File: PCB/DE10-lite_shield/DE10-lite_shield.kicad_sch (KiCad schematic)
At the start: 4 parts

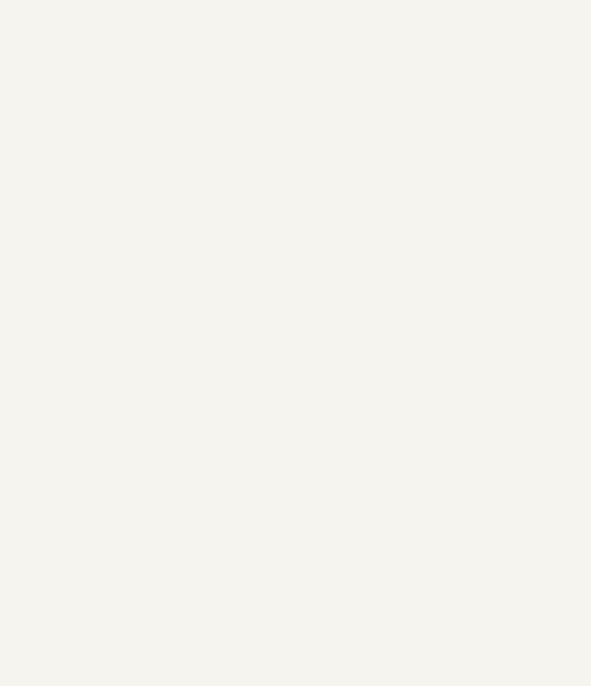
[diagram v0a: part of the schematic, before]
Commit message: Updated PCB dimensions
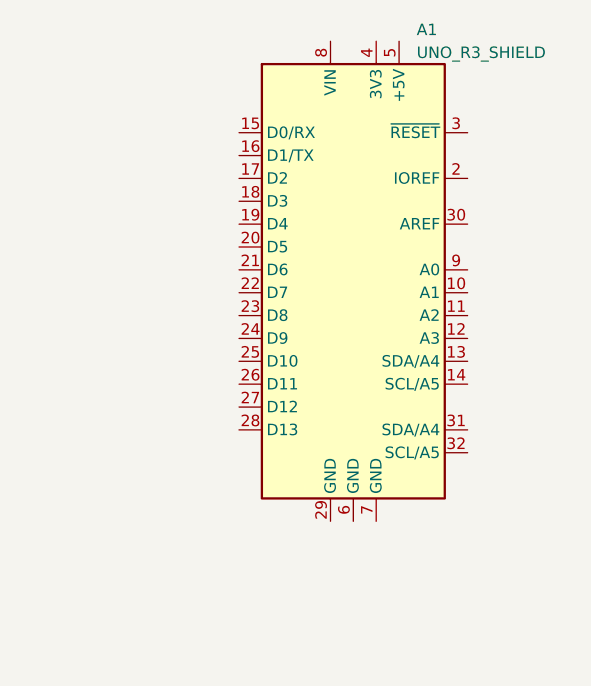
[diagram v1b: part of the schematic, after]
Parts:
- added A1: UNO_R3_SHIELD, footprints:UNO_R3_SHIELD, symbol Personal Library:UNO_R3_SHIELD
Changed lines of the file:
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@@
+    )
+  )
+  (symbol (lib_id "Personal Library:UNO_R3_SHIELD") (at 118.11 97.79 0) (unit 1)
+    (in_bom yes) (on_board yes) (dnp no) (fields_autoplaced)
+    (property "Reference" "A1" (at 125.1459 71.12 0)
+      (effects (font (size 1.27 1.27)) (justify left))
+    )
+    (property "Value" "UNO_R3_SHIELD" (at 125.1459 73.66 0)
+      (effects (font (size 1.27 1.27)) (justify left))
+    )
+    (property "Footprint" "footprints:UNO_R3_SHIELD" (at 118.11 97.79 0)
+      (effects (font (size 1.27 1.27) italic) hide)
+    )
+    (property "Datasheet" "https://www.arduino.cc/en/Main/arduinoBoardUno" (at 118.11 97.79 0)
+      (effects (font (size 1.27 1.27)) hide)
+    )
+    (pin "1")
+    (pin "10")
+    (pin "11")
+    (pin "12")
+    (pin "13")
+    (pin "14")
+    (pin "15")
+    (pin "16")
+    (pin "17")
+    (pin "18")
+    (pin "19")
+    (pin "2")
+    (pin "20")
+    (pin "21")
+    (pin "22")
+    (pin "23")
+    (pin "24")
+    (pin "25")
+    (pin "26")
+    (pin "27")
+    (pin "28")
+    (pin "29")
+    (pin "3")
+    (pin "30")
+    (pin "31")
+    (pin "32")
+    (pin "4")
+    (pin "5")
+    (pin "6")
+    (pin "7")
+    (pin "8")
+    (pin "9")
+    (instances
+      (project "DE10-lite_shield"
+        (path "/42dcd1c6-b27b-471e-adaa-a184b6e8160d"
+          (reference "A1") (unit 1)
+        )
+      )
     )
   )

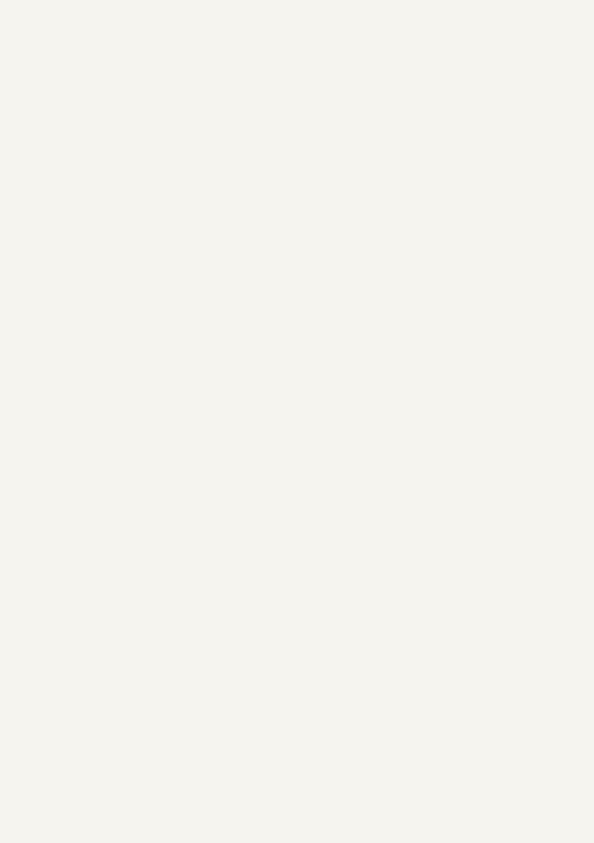
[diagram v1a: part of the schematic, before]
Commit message: Updated .gitignore
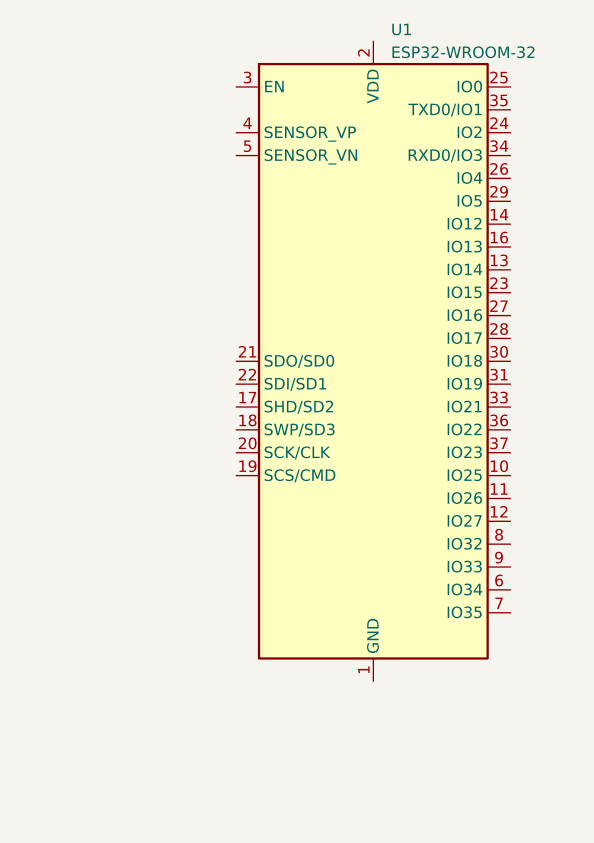
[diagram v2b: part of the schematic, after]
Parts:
- added U1: ESP32-WROOM-32, RF_Module:ESP32-WROOM-32, symbol RF_Module:ESP32-WROOM-32
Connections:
- new net: U1.1 (GND), U1.15 (GND), U1.38 (GND), U1.39 (GND)
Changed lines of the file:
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@@
+    )
+  )
+  (symbol (lib_id "RF_Module:ESP32-WROOM-32") (at 198.12 93.98 0) (unit 1)
+    (in_bom yes) (on_board yes) (dnp no) (fields_autoplaced)
+    (property "Reference" "U1" (at 200.0759 57.15 0)
+      (effects (font (size 1.27 1.27)) (justify left))
+    )
+    (property "Value" "ESP32-WROOM-32" (at 200.0759 59.69 0)
+      (effects (font (size 1.27 1.27)) (justify left))
+    )
+    (property "Footprint" "RF_Module:ESP32-WROOM-32" (at 198.12 132.08 0)
+      (effects (font (size 1.27 1.27)) hide)
+    )
+    (property "Datasheet" "https://www.espressif.com/sites/default/files/documentation/esp32-wroom-32_datasheet_en.pdf" (at 190.5 92.71 0)
+      (effects (font (size 1.27 1.27)) hide)
+    )
+    (pin "1")
+    (pin "10")
+    (pin "11")
+    (pin "12")
+    (pin "13")
+    (pin "14")
+    (pin "15")
+    (pin "16")
+    (pin "17")
+    (pin "18")
+    (pin "19")
+    (pin "2")
+    (pin "20")
+    (pin "21")
+    (pin "22")
+    (pin "23")
+    (pin "24")
+    (pin "25")
+    (pin "26")
+    (pin "27")
+    (pin "28")
+    (pin "29")
+    (pin "3")
+    (pin "30")
+    (pin "31")
+    (pin "32")
+    (pin "33")
+    (pin "34")
+    (pin "35")
+    (pin "36")
+    (pin "37")
+    (pin "38")
+    (pin "39")
+    (pin "4")
+    (pin "5")
+    (pin "6")
+    (pin "7")
+    (pin "8")
+    (pin "9")
+    (instances
+      (project "DE10-lite_shield"
+        (path "/42dcd1c6-b27b-471e-adaa-a184b6e8160d"
+          (reference "U1") (unit 1)
+        )
+      )
     )
   )

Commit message: PCB almost done
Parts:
- added A2, A3: Pololu_Breakout_A4988, Module:Pololu_Breakout-16_15.2x20.3mm, symbol Driver_Motor:Pololu_Breakout_A4988
- added C1, C2: 100u, Capacitor_THT:C_Rect_L4.0mm_W2.5mm_P2.50mm, symbol Device:C_Polarized_Small
- added C10, C11, C19, C20: 10n, Capacitor_SMD:C_0402_1005Metric, symbol Device:C_Small
- added C12, C14, C17, C18, C22, C23, C3, C4: 100n, Capacitor_SMD:C_0402_1005Metric, symbol Device:C_Small
- added C13: 4u7, Capacitor_SMD:C_0402_1005Metric, symbol Device:C_Small
- added C15, C16, C21, C24, C8, C9: 10u, Capacitor_SMD:C_0402_1005Metric, symbol Device:C_Small
- added C5: 1u, Capacitor_SMD:C_0402_1005Metric, symbol Device:C_Small
- added C6, C7: 47u, Capacitor_SMD:C_0805_2012Metric, symbol Device:C_Small
- added D1: BAT760-115, Diode_SMD:D_SOD-323, symbol Device:D_Schottky
- added D2, D3: LED_R, LED_SMD:LED_0603_1608Metric, symbol Device:LED_Small
- added D4, D5: LED_B, LED_SMD:LED_0603_1608Metric, symbol Device:LED_Small
- added F1: Fuse, Fuse:Fuseholder_Cylinder-5x20mm_Schurter_0031_8201_Horizontal_Open, symbol Device:Fuse
- added J1, J2: Conn_01x04, Connector_PinHeader_2.54mm:PinHeader_1x04_P2.54mm_Vertical, symbol Connector_Generic:Conn_01x04
- added J10: Conn_01x02, Connector_PinHeader_2.54mm:PinHeader_1x02_P2.54mm_Vertical, symbol Connector_Generic:Conn_01x02
- added J11, J12: SM04B-SRSS-TB(LF)(SN), footprints:JST_SM04B-SRSS-TB(LF)(SN), symbol SM04B-SRSS-TB_LF__SN_:SM04B-SRSS-TB(LF)(SN)
- added J3: Screw_Terminal_01x02, TerminalBlock:TerminalBlock_bornier-2_P5.08mm, symbol Connector:Screw_Terminal_01x02
- added J4: USB4056-03-A, footprints:GCT_USB4056-03-A_REVA, symbol USB4056-03-A:USB4056-03-A
- added J5, J6, J7, J8: Conn_01x05, Connector_PinHeader_2.54mm:PinHeader_1x05_P2.54mm_Vertical, symbol Connector_Generic:Conn_01x05
- added J9: Conn_01x03, Connector_PinHeader_2.54mm:PinHeader_1x03_P2.54mm_Vertical, symbol Connector_Generic:Conn_01x03
- added JP1, JP2, JP3, JP4, JP5, JP6, JP7, JP8: Jumper_2_Open, Connector_PinHeader_2.54mm:PinHeader_1x02_P2.54mm_Vertical, symbol Jumper:Jumper_2_Open
- added L1: 3u3, footprints:INDPM3630X200N, symbol Device:L_Small
- added L2: 2u2, footprints:INDPM3630X200N, symbol Device:L_Small
- added Q1, Q2: S8050, footprints:S8050, symbol Transistor_BJT:S8050
- added R1, R2: R_Small, Resistor_SMD:R_0402_1005Metric, symbol Device:R_Small
- added R10, R30, R5, R6: 4k7, Resistor_SMD:R_0402_1005Metric, symbol Device:R_Small
- added R11, R12, R13, R14, R15, R18, R20, R21, R22, R23, R27, R31, R4, R7, R8: 10k, Resistor_SMD:R_0402_1005Metric, symbol Device:R_Small
- added R16, R17, R24, R9: 2k2, Resistor_SMD:R_0402_1005Metric, symbol Device:R_Small
- added R19: 3k3, Resistor_SMD:R_0402_1005Metric, symbol Device:R_Small
- added R25, R26, R28: 1k5, Resistor_SMD:R_0402_1005Metric, symbol Device:R_Small
- added R3: 33k, Resistor_SMD:R_0402_1005Metric, symbol Device:R_Small
- added S1, S2: TS20-42-25-WT-160-SMT-TR, footprints:TS204225WT160SMTTR, symbol TS20-42-25-WT-160-SMT-TR:TS20-42-25-WT-160-SMT-TR
- added SW1: SW_DPDT_x2, Connector_PinHeader_2.54mm:PinHeader_1x03_P2.54mm_Vertical, symbol Switch:SW_DPDT_x2
- added U2: CP2102N-Axx-xQFN28, Package_DFN_QFN:QFN-28-1EP_5x5mm_P0.5mm_EP3.35x3.35mm, symbol Interface_USB:CP2102N-Axx-xQFN28
- added U3: TPS54295RSAT, footprints:TPS54295RSAT, symbol TPS54295RSAT:TPS54295RSAT
- added U4: TCA9548AMRGER, Package_DFN_QFN:Texas_RGE0024C_EP2.1x2.1mm, symbol Interface_Expansion:TCA9548AMRGER
- added U5: ICM-20948, Sensor_Motion:InvenSense_QFN-24_3x3mm_P0.4mm, symbol Sensor_Motion:ICM-20948
- added U7: MIC5504-1.8YM5, Package_TO_SOT_SMD:SOT-23-5, symbol Regulator_Linear:MIC5504-1.8YM5
- added U8: TXS0108EPW, Package_SO:TSSOP-20_4.4x6.5mm_P0.65mm, symbol Logic_LevelTranslator:TXS0108EPW
- added U9: TPD4S012, footprints:SON50P100X145X60-6_TPD4S012DRYR, symbol TPD4S012:TPD4S012
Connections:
- net GND: now also A1.29 (GND), U1.1 (GND), U1.15 (GND), U1.38 (GND), U1.39 (GND), A2.1 (GND), A2.7 (GND), A3.1 (GND), A3.7 (GND), C1.2, C10.1, C11.1, C12.2, C13.2, C14.2, C15.2, C16.2, C17.2, C18.2, C19.2, C2.2, C20.2, C21.2, C22.2, C23.2, C24.2, C5.2, C6.2, C7.2, C8.2, C9.2, J10.2 (Pin_2), J11.1, J11.S1 (SHIELD), J11.S2 (SHIELD), J12.1, J12.S1 (SHIELD), J12.S2 (SHIELD), J3.1 (Pin_1), J4.A1 (GND), J4.A12 (GND), J4.B1 (GND), J4.B12 (GND), J4.S1 (SHIELD), J4.S2 (SHIELD), J4.S3 (SHIELD), J4.S4 (SHIELD), J5.2 (Pin_2), J6.2 (Pin_2), J7.2 (Pin_2), J8.2 (Pin_2), J9.3 (Pin_3), R11.2, R12.1, R13.1, R14.1, R19.2, R2.2, R22.2, R24.2, R25.2, R26.2, R28.2, R31.2, R4.2, R5.2, R6.2, S1.3 (COM_1), S2.3 (COM_1), U2.29 (GND), U2.3 (GND), U3.10 (GND), U3.15 (PGND2), U3.17 (PAD), U3.6 (PGND1), U4.9 (GND), U5.18 (GND), U5.20 (GND), U7.2 (GND), U8.11 (GND), U9.4 (GND)
- net FPGA_INT: now reaches U1.10 (IO25)
- net FPGA_INT: now also A1.28 (D13)
- net FPGA_GPIO: now reaches U1.11 (IO26)
- net FPGA_GPIO: now also A1.27 (D12)
- net ESP32_LED_A: now reaches U1.12 (IO27)
- net ESP32_LED_A: now also D4.2 (A)
- net SERVO: now reaches U1.16 (IO13)
- net SERVO: now also J9.1 (Pin_1)
- net +3V3: now reaches U1.2 (VDD)
- net +3V3: now also A2.2 (VDD), A3.2 (VDD), C12.1, C13.1, C14.1, C15.1, C21.1, C22.1, C24.1, C6.1, D3.2 (A), J11.2, J12.2, J5.1 (Pin_1), J6.1 (Pin_1), J7.1 (Pin_1), J8.1 (Pin_1), JP1.1 (A), JP2.1 (A), JP3.1 (A), JP4.1 (A), JP5.1 (A), JP6.1 (A), L2.2, R15.2, R16.2, R17.2, R23.2, R27.2, R3.1, R9.2, U2.6 (VDD), U2.7 (VREGIN), U4.21 (VCC), U7.1 (VIN), U7.3 (EN), U8.19 (VCCB)
- net I2C3_INT: now reaches U1.23 (IO15)
- net I2C3_INT: now also J8.5 (Pin_5)
- net I2C2_INT: now reaches U1.24 (IO2)
- net I2C2_INT: now also J7.5 (Pin_5)
- net IO0: now reaches U1.25 (IO0)
- net IO0: now also C19.1, Q2.3 (C), R27.1, S1.2 (NO_2)
- net MOTOR1_STEP: now reaches U1.26 (IO4)
- net MOTOR1_STEP: now also A3.15 (STEP), JP8.1 (A)
- net MOTOR2_DIR: now reaches U1.27 (IO16)
- net MOTOR2_DIR: now also A2.16 (DIR)
- net IMU_INT: now reaches U1.28 (IO17)
- net IMU_INT: now also U8.16 (B4)
- net CS: now reaches U1.29 (IO5)
- net CS: now also U8.17 (B3)
- net EN: now reaches U1.3 (EN)
- net EN: now also C20.1, Q1.3 (C), R23.1, S2.2 (NO_2)
- net SCK: now reaches U1.30 (IO18)
- net SCK: now also U8.18 (B2)
- net MISO: now reaches U1.31 (IO19)
- net MISO: now also U8.15 (B5)
- net ESP32_SDA: now reaches U1.33 (IO21)
- net ESP32_SDA: now also A1.31 (SDA/D14), R17.1, U4.20 (SDA)
- net ESP32_RX: now reaches U1.34 (RXD0/IO3)
- net ESP32_RX: now also A1.16 (D1/TX), U2.26 (TXD)
- net ESP32_TX: now reaches U1.35 (TXD0/IO1)
- net ESP32_TX: now also A1.15 (D0/RX), U2.25 (RXD)
- net ESP32_SCL: now reaches U1.36 (IO22)
- net ESP32_SCL: now also A1.32 (SCL/D15), R16.1, U4.19 (SCL)
- net MOSI: now reaches U1.37 (IO23)
- net MOSI: now also U8.20 (B1)
- net BATT/4: now reaches U1.4 (SENSOR_VP)
- net BATT/4: now also R19.1, R20.2
- net VBUS/2: now reaches U1.5 (SENSOR_VN)
- net VBUS/2: now also R21.2, R22.1
- net I2C0_INT: now reaches U1.6 (IO34)
- net I2C0_INT: now also J5.5 (Pin_5)
- net I2C1_INT: now reaches U1.7 (IO35)
- net I2C1_INT: now also J6.5 (Pin_5)
- net MOTOR1_DIR: now reaches U1.8 (IO32)
- net MOTOR1_DIR: now also A3.16 (DIR)
- net MOTOR2_STEP: now reaches U1.9 (IO33)
- net MOTOR2_STEP: now also JP7.1 (A)
- net FPGA_LED_A: now reaches A1.26 (D11)
- net FPGA_LED_A: now also D5.2 (A)
- new net +1V8: C16.1, C17.1, C23.1, R18.2, U5.13 (VDD), U5.8 (VDDIO), U7.5 (VOUT), U8.2 (VCCA)
- new net +5V: C7.1, D2.2 (A), J10.1 (Pin_1), J9.2 (Pin_2), L1.2, R1.1
- new net +BATT: A2.8 (VMOT), A3.8 (VMOT), C1.1, C2.1, C8.1, C9.1, D1.1 (K), R20.1, SW1.2 (B), U3.14 (EN2), U3.2 (VIN2), U3.3 (VIN1), U3.7 (EN1)
- new net CC1: J4.A5 (CC1), R6.1
- new net CC2: J4.B5 (CC2), R5.1
- new net CS_1V8: U5.22 (~{CS}), U8.4 (A3)
- new net DN: J4.A7 (D-), J4.B7 (D-), U2.5 (D-), U9.1 (D+)
- new net DP: J4.A6 (D+), J4.B6 (D+), U2.4 (D+), U9.2 (D-)
- new net DTR: Q2.1 (E), R7.1, U2.28 (~{DTR})
- new net DTR_B: Q1.2 (B), R7.2
- new net ESP32_LED_K: D4.1 (K), R26.1
- new net FPGA_LED_K: D5.1 (K), R28.1
- new net IMU_INT_1V8: U5.12 (INT1), U8.5 (A4)
- new net LED_3V3: D3.1 (K), R25.1
- new net LED_5V: D2.1 (K), R24.1
- new net MISO_1V8: U5.9 (SDO/AD0), U8.6 (A5)
- new net MOSI_1V8: U5.24 (SDA/SDI), U8.1 (A1)
- new net MOTOR1_1A: A3.4 (1A), J1.2 (Pin_2)
- new net MOTOR1_1B: A3.3 (1B), J1.1 (Pin_1)
- new net MOTOR1_2A: A3.5 (2A), J1.3 (Pin_3)
- new net MOTOR1_2B: A3.6 (2B), J1.4 (Pin_4)
- new net MOTOR1_MS1: A3.10 (MS1), JP1.2 (B)
- new net MOTOR1_MS2: A3.11 (MS2), JP2.2 (B)
- new net MOTOR1_MS3: A3.12 (MS3), JP3.2 (B)
- new net MOTOR1_RST: A3.13 (~{RESET}), A3.14 (~{SLEEP})
- new net MOTOR2_1A: A2.4 (1A), J2.2 (Pin_2)
- new net MOTOR2_1B: A2.3 (1B), J2.1 (Pin_1)
- new net MOTOR2_2A: A2.5 (2A), J2.3 (Pin_3)
- new net MOTOR2_2B: A2.6 (2B), J2.4 (Pin_4)
- new net MOTOR2_MS1: A2.10 (MS1), JP4.2 (B)
- new net MOTOR2_MS2: A2.11 (MS2), JP5.2 (B)
- new net MOTOR2_MS3: A2.12 (MS3), JP6.2 (B)
- new net MOTOR2_RST: A2.13 (~{RESET}), A2.14 (~{SLEEP})
- new net MOTOR2_STEP_IN: A2.15 (STEP), JP7.2 (B), JP8.2 (B)
- new net MOTOR_EN: A2.9 (~{ENABLE}), A3.9 (~{ENABLE}), R30.2, R31.1
- new net REGOUT: C18.1, U5.10 (REGOUT)
- new net RTS: Q1.1 (E), R8.1, U2.24 (~{RTS})
- new net RTS_B: Q2.2 (B), R8.2
- new net SCK_1V8: U5.23 (SCL/SCLK), U8.3 (A2)
- new net SCL0: J5.3 (Pin_3), U4.2 (SC0)
- new net SCL1: J6.3 (Pin_3), U4.4 (SC1)
- new net SCL2: J7.3 (Pin_3), U4.6 (SC2)
- new net SCL3: J8.3 (Pin_3), U4.8 (SC3)
- new net SCL4: J11.3, U4.11 (SC4)
- new net SCL5: J12.3, U4.13 (SC5)
- new net SDA0: J5.4 (Pin_4), U4.1 (SD0)
- new net SDA1: J6.4 (Pin_4), U4.3 (SD1)
- new net SDA2: J7.4 (Pin_4), U4.5 (SD2)
- new net SDA3: J8.4 (Pin_4), U4.7 (SD3)
- new net SDA4: J11.4, U4.10 (SD4)
- new net SDA5: J12.4, U4.12 (SD5)
- new net SS1: C10.2, U3.8 (SS1)
- new net SS2: C11.2, U3.13 (SS2)
- new net SW1: C3.2, L1.1, U3.5 (SW1)
- new net SW2: C4.2, L2.1, U3.16 (SW2)
- new net SW3: R30.1, SW1.3 (C)
- new net TCA_A0: R14.2, U4.22 (A0)
- new net TCA_A1: R13.2, U4.23 (A1)
- new net TCA_A2: R12.2, U4.18 (A2)
- new net TCA_RST: R15.1, U4.24 (~{RESET})
- new net TXS_OE: R18.1, U8.10 (OE)
- new net USB_RST: R9.1, U2.9 (~{RST})
- new net USB_VBUS: R10.2, R11.1, U2.8 (VBUS)
- new net VBST1: C3.1, U3.4 (VBST1)
- new net VBST2: C4.1, U3.1 (VBST2)
- new net VBUS: D1.2 (A), J4.A4 (VBUS), J4.A9 (VBUS), J4.B4 (VBUS), J4.B9 (VBUS), R10.1, R21.1, U9.6 (VBUS)
- new net VFB1: R1.2, R2.1, U3.9 (VFB1)
- new net VFB2: R3.2, R4.1, U3.12 (VFB2)
- new net VIN: F1.1, J3.2 (Pin_2)
- new net VIN_FUSED: F1.2, SW1.1 (A)
- new net VREG5: C5.1, U3.11 (VREG5)
- no-connect marks 0 -> 61
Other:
- note added: "Ensures the motors are turned off when the switch is flipped"
- note added: "FPGA Power"
- note added: "Jumper to decide whether motor 2 is fed by the same step pin as motor 1"
- note added: "Servo"
- note added: "Servo header"
- note added: "Use 10V caps on VIN"
- moved on the sheet: H1, H2, H3, H4, U1

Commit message: FINISHED CIRCUIT BOARD IN 24 HOURS
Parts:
- removed JP7, JP8: Jumper_2_Open, Connector_PinHeader_2.54mm:PinHeader_1x02_P2.54mm_Vertical, symbol Jumper:Jumper_2_Open
- added JP9: Jumper_3_Open, Connector_PinHeader_2.54mm:PinHeader_1x03_P2.54mm_Vertical, symbol Jumper:Jumper_3_Open
- SW1: footprint Connector_PinHeader_2.54mm:PinHeader_1x03_P2.54mm_Vertical -> footprints:Toggle_switch
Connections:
- net GND: no longer J11.S1 (SHIELD), J11.S2 (SHIELD), J12.S1 (SHIELD), J12.S2 (SHIELD)
- net MOTOR1_1A: now also A2.4 (1A), J2.2 (Pin_2); no longer A3.4 (1A), J1.2 (Pin_2)
- net MOTOR1_1B: now also A2.3 (1B), J2.1 (Pin_1); no longer A3.3 (1B), J1.1 (Pin_1)
- net MOTOR1_2A: now also A2.5 (2A), J2.3 (Pin_3); no longer A3.5 (2A), J1.3 (Pin_3)
- net MOTOR1_2B: now also A2.6 (2B), J2.4 (Pin_4); no longer A3.6 (2B), J1.4 (Pin_4)
- net MOTOR1_DIR: now also A2.16 (DIR), U1.27 (IO16); no longer A3.16 (DIR), U1.8 (IO32)
- net MOTOR1_MS1: now also A2.10 (MS1), JP4.2 (B); no longer A3.10 (MS1), JP1.2 (B)
- net MOTOR1_MS2: now also A2.11 (MS2), JP5.2 (B); no longer A3.11 (MS2), JP2.2 (B)
- net MOTOR1_MS3: now also A2.12 (MS3), JP6.2 (B); no longer A3.12 (MS3), JP3.2 (B)
- net MOTOR1_RST: now also A2.13 (~{RESET}), A2.14 (~{SLEEP}); no longer A3.13 (~{RESET}), A3.14 (~{SLEEP})
- net MOTOR1_STEP: now also A2.15 (STEP), JP9.1 (A); no longer A3.15 (STEP)
- net MOTOR2_1A: now also A3.4 (1A), J1.2 (Pin_2); no longer A2.4 (1A), J2.2 (Pin_2)
- net MOTOR2_1B: now also A3.3 (1B), J1.1 (Pin_1); no longer A2.3 (1B), J2.1 (Pin_1)
- net MOTOR2_2A: now also A3.5 (2A), J1.3 (Pin_3); no longer A2.5 (2A), J2.3 (Pin_3)
- net MOTOR2_2B: now also A3.6 (2B), J1.4 (Pin_4); no longer A2.6 (2B), J2.4 (Pin_4)
- net MOTOR2_DIR: now also A3.16 (DIR), U1.8 (IO32); no longer A2.16 (DIR), U1.27 (IO16)
- net MOTOR2_MS1: now also A3.10 (MS1), JP1.2 (B); no longer A2.10 (MS1), JP4.2 (B)
- net MOTOR2_MS2: now also A3.11 (MS2), JP2.2 (B); no longer A2.11 (MS2), JP5.2 (B)
- net MOTOR2_MS3: now also A3.12 (MS3), JP3.2 (B); no longer A2.12 (MS3), JP6.2 (B)
- net MOTOR2_RST: now also A3.13 (~{RESET}), A3.14 (~{SLEEP}); no longer A2.13 (~{RESET}), A2.14 (~{SLEEP})
- net MOTOR2_STEP: now also JP9.3 (B)
- net MOTOR2_STEP_IN: now also A3.15 (STEP), JP9.2 (C); no longer A2.15 (STEP)
- new net: J11.S1 (SHIELD), J11.S2 (SHIELD)
- new net: J12.S1 (SHIELD), J12.S2 (SHIELD)
- no-connect marks 61 -> 64

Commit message: Finished PCB
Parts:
- Q1: footprint footprints:S8050 -> Package_TO_SOT_THT:TO-92_Inline
- R1: value R_Small -> 124k
- R2: value R_Small -> 22k1
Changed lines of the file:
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@@
       (effects (font (size 1.27 1.27)) (justify left))
     )
-    (property "Value" "R_Small" (at 127 74.295 0)
+    (property "Value" "22k1" (at 127 74.295 0)
       (effects (font (size 1.27 1.27)) (justify left))
     )
@@
       (effects (font (size 1.27 1.27)) (justify left))
     )
-    (property "Value" "R_Small" (at 127 64.135 0)
+    (property "Value" "124k" (at 127 64.135 0)
       (effects (font (size 1.27 1.27)) (justify left))
     )
@@
       (effects (font (size 1.27 1.27)) (justify left))
     )
-    (property "Footprint" "footprints:S8050" (at 189.23 170.815 0)
+    (property "Footprint" "Package_TO_SOT_THT:TO-92_Inline" (at 189.23 170.815 0)
       (effects (font (size 1.27 1.27) italic) (justify left) hide)
     )

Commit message: Updated pcb schematic
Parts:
- removed A1: UNO_R3_SHIELD, footprints:UNO_R3_SHIELD, symbol Personal Library:UNO_R3_SHIELD
- removed A2, A3: Pololu_Breakout_A4988, Module:Pololu_Breakout-16_15.2x20.3mm, symbol Driver_Motor:Pololu_Breakout_A4988
- removed C1, C2: 100u, Capacitor_THT:C_Rect_L4.0mm_W2.5mm_P2.50mm, symbol Device:C_Polarized_Small
- removed C10, C11, C19, C20: 10n, Capacitor_SMD:C_0402_1005Metric, symbol Device:C_Small
- removed C12, C14, C17, C18, C22, C23, C3, C4: 100n, Capacitor_SMD:C_0402_1005Metric, symbol Device:C_Small
- removed C13: 4u7, Capacitor_SMD:C_0402_1005Metric, symbol Device:C_Small
- removed C15, C16, C21, C24, C8, C9: 10u, Capacitor_SMD:C_0402_1005Metric, symbol Device:C_Small
- removed C5: 1u, Capacitor_SMD:C_0402_1005Metric, symbol Device:C_Small
- removed C6, C7: 47u, Capacitor_SMD:C_0805_2012Metric, symbol Device:C_Small
- removed D1: BAT760-115, Diode_SMD:D_SOD-323, symbol Device:D_Schottky
- removed D2, D3: LED_R, LED_SMD:LED_0603_1608Metric, symbol Device:LED_Small
- removed D4, D5: LED_B, LED_SMD:LED_0603_1608Metric, symbol Device:LED_Small
- removed F1: Fuse, Fuse:Fuseholder_Cylinder-5x20mm_Schurter_0031_8201_Horizontal_Open, symbol Device:Fuse
- removed H1, H2, H3, H4: MountingHole_Pad, MountingHole:MountingHole_3.2mm_M3_DIN965_Pad, symbol Mechanical:MountingHole_Pad
- removed J1, J2: Conn_01x04, Connector_PinHeader_2.54mm:PinHeader_1x04_P2.54mm_Vertical, symbol Connector_Generic:Conn_01x04
- removed J10: Conn_01x02, Connector_PinHeader_2.54mm:PinHeader_1x02_P2.54mm_Vertical, symbol Connector_Generic:Conn_01x02
- removed J11, J12: SM04B-SRSS-TB(LF)(SN), footprints:JST_SM04B-SRSS-TB(LF)(SN), symbol SM04B-SRSS-TB_LF__SN_:SM04B-SRSS-TB(LF)(SN)
- removed J3: Screw_Terminal_01x02, TerminalBlock:TerminalBlock_bornier-2_P5.08mm, symbol Connector:Screw_Terminal_01x02
- removed J4: USB4056-03-A, footprints:GCT_USB4056-03-A_REVA, symbol USB4056-03-A:USB4056-03-A
- removed J5, J6, J7, J8: Conn_01x05, Connector_PinHeader_2.54mm:PinHeader_1x05_P2.54mm_Vertical, symbol Connector_Generic:Conn_01x05
- removed J9: Conn_01x03, Connector_PinHeader_2.54mm:PinHeader_1x03_P2.54mm_Vertical, symbol Connector_Generic:Conn_01x03
- removed JP1, JP2, JP3, JP4, JP5, JP6: Jumper_2_Open, Connector_PinHeader_2.54mm:PinHeader_1x02_P2.54mm_Vertical, symbol Jumper:Jumper_2_Open
- removed JP9: Jumper_3_Open, Connector_PinHeader_2.54mm:PinHeader_1x03_P2.54mm_Vertical, symbol Jumper:Jumper_3_Open
- removed L1: 3u3, footprints:INDPM3630X200N, symbol Device:L_Small
- removed L2: 2u2, footprints:INDPM3630X200N, symbol Device:L_Small
- removed Q1: S8050, Package_TO_SOT_THT:TO-92_Inline, symbol Transistor_BJT:S8050
- removed Q2: S8050, footprints:S8050, symbol Transistor_BJT:S8050
- removed R1: 124k, Resistor_SMD:R_0402_1005Metric, symbol Device:R_Small
- removed R10, R30, R5, R6: 4k7, Resistor_SMD:R_0402_1005Metric, symbol Device:R_Small
- removed R11, R12, R13, R14, R15, R18, R20, R21, R22, R23, R27, R31, R4, R7, R8: 10k, Resistor_SMD:R_0402_1005Metric, symbol Device:R_Small
- removed R16, R17, R24, R9: 2k2, Resistor_SMD:R_0402_1005Metric, symbol Device:R_Small
- removed R19: 3k3, Resistor_SMD:R_0402_1005Metric, symbol Device:R_Small
- removed R2: 22k1, Resistor_SMD:R_0402_1005Metric, symbol Device:R_Small
- removed R25, R26, R28: 1k5, Resistor_SMD:R_0402_1005Metric, symbol Device:R_Small
- removed R3: 33k, Resistor_SMD:R_0402_1005Metric, symbol Device:R_Small
- removed S1, S2: TS20-42-25-WT-160-SMT-TR, footprints:TS204225WT160SMTTR, symbol TS20-42-25-WT-160-SMT-TR:TS20-42-25-WT-160-SMT-TR
- removed SW1: SW_DPDT_x2, footprints:Toggle_switch, symbol Switch:SW_DPDT_x2
- removed U1: ESP32-WROOM-32, RF_Module:ESP32-WROOM-32, symbol RF_Module:ESP32-WROOM-32
- removed U2: CP2102N-Axx-xQFN28, Package_DFN_QFN:QFN-28-1EP_5x5mm_P0.5mm_EP3.35x3.35mm, symbol Interface_USB:CP2102N-Axx-xQFN28
- removed U3: TPS54295RSAT, footprints:TPS54295RSAT, symbol TPS54295RSAT:TPS54295RSAT
- removed U4: TCA9548AMRGER, Package_DFN_QFN:Texas_RGE0024C_EP2.1x2.1mm, symbol Interface_Expansion:TCA9548AMRGER
- removed U5: ICM-20948, Sensor_Motion:InvenSense_QFN-24_3x3mm_P0.4mm, symbol Sensor_Motion:ICM-20948
- removed U7: MIC5504-1.8YM5, Package_TO_SOT_SMD:SOT-23-5, symbol Regulator_Linear:MIC5504-1.8YM5
- removed U8: TXS0108EPW, Package_SO:TSSOP-20_4.4x6.5mm_P0.65mm, symbol Logic_LevelTranslator:TXS0108EPW
- removed U9: TPD4S012, footprints:SON50P100X145X60-6_TPD4S012DRYR, symbol TPD4S012:TPD4S012
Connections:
- no-connect marks 64 -> 0
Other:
- added sheet Microcontroller & USB (microcontroller_usb.kicad_sch)
- added sheet Other (other.kicad_sch)
- added sheet Power (power.kicad_sch)
- added sheet Sensors (sensors.kicad_sch)
- note removed: "Ensures the motors are turned off when the switch is flipped"
- note removed: "FPGA Power"
- note removed: "Jumper to decide whether motor 2 is fed by the same step pin as motor 1"
- note removed: "Servo"
- note removed: "Servo header"
- note removed: "Use 10V caps on VIN"
